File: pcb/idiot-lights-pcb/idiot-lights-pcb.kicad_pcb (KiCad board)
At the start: 2 copper layers, 100.3 x 64.1 mm, 103 parts, among them Q1 BSS138, Q10 BSS138, Q11 BSS138, Q12 BSS138, Q13 BSS138, Q14 BSS138, Q15 BSS138, Q16 BSS138, Q2 BSS138, Q3 BSS138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

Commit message: Fix resistor values
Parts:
- R10, R12, R14, R16, R18, R2, R20, R22, R24, R26, R28, R30, R32, R4, R6, R8: value 150 -> 330
- R33, R34, R35, R36, R37, R38, R39, R40, R41, R42, R43, R44, R45, R46, R47, R48: value 3k3 -> 1500
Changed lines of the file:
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@@
         (effects (font (size 1 1) (thickness 0.15)))
     )
-    (fp_text value "150" (at 0 1.43 180) (layer "F.Fab")
+    (fp_text value "330" (at 0 1.43 180) (layer "F.Fab")
         (effects (font (size 1 1) (thickness 0.15)))
     )
@@
         (effects (font (size 1 1) (thickness 0.15)))
     )
-    (fp_text value "150" (at 0 1.43 180) (layer "F.Fab")
+    (fp_text value "330" (at 0 1.43 180) (layer "F.Fab")
         (effects (font (size 1 1) (thickness 0.15)))
     )
@@
         (effects (font (size 1 1) (thickness 0.15)))
     )
-    (fp_text value "3k3" (at 0 1.43) (layer "F.Fab")
+    (fp_text value "1500" (at 0 1.43) (layer "F.Fab")
         (effects (font (size 1 1) (thickness 0.15)))
     )
@@
         (effects (font (size 1 1) (thickness 0.15)))
     )
-    (fp_text value "3k3" (at 0 1.43) (layer "F.Fab")
+    (fp_text value "1500" (at 0 1.43) (layer "F.Fab")
         (effects (font (size 1 1) (thickness 0.15)))
     )
@@
         (effects (font (size 1 1) (thickness 0.15)))
     )
-    (fp_text value "150" (at 0 1.43) (layer "F.Fab")
+    (fp_text value "330" (at 0 1.43) (layer "F.Fab")
         (effects (font (size 1 1) (thickness 0.15)))
     )
@@
         (effects (font (size 1 1) (thickness 0.15)))
     )
-    (fp_text value "3k3" (at 0 1.43) (layer "F.Fab")
+    (fp_text value "1500" (at 0 1.43) (layer "F.Fab")
         (effects (font (size 1 1) (thickness 0.15)))
     )
@@
         (effects (font (size 1 1) (thickness 0.15)))
     )
-    (fp_text value "3k3" (at 0 1.43) (layer "F.Fab")
+    (fp_text value "1500" (at 0 1.43) (layer "F.Fab")
         (effects (font (size 1 1) (thickness 0.15)))
     )
@@
         (effects (font (size 1 1) (thickness 0.15)))
     )
-    (fp_text value "3k3" (at 0 1.43) (layer "F.Fab")
+    (fp_text value "1500" (at 0 1.43) (layer "F.Fab")
         (effects (font (size 1 1) (thickness 0.15)))
     )
@@
         (effects (font (size 1 1) (thickness 0.15)))
     )
-    (fp_text value "3k3" (at 0 1.43) (layer "F.Fab")
+    (fp_text value "1500" (at 0 1.43) (layer "F.Fab")
         (effects (font (size 1 1) (thickness 0.15)))
     )
@@
         (effects (font (size 1 1) (thickness 0.15)))
     )
-    (fp_text value "3k3" (at 0 1.43) (layer "F.Fab")
+    (fp_text value "1500" (at 0 1.43) (layer "F.Fab")
         (effects (font (size 1 1) (thickness 0.15)))
     )
@@
         (effects (font (size 1 1) (thickness 0.15)))
     )
-    (fp_text value "150" (at 0 1.43 180) (layer "F.Fab")
+    (fp_text value "330" (at 0 1.43 180) (layer "F.Fab")
         (effects (font (size 1 1) (thickness 0.15)))
     )
@@
         (effects (font (size 1 1) (thickness 0.15)))
     )
-    (fp_text value "150" (at 0 1.43) (layer "F.Fab")
+    (fp_text value "330" (at 0 1.43) (layer "F.Fab")
         (effects (font (size 1 1) (thickness 0.15)))
     )
@@
         (effects (font (size 1 1) (thickness 0.15)))
     )
-    (fp_text value "150" (at 0 1.43) (layer "F.Fab")
+    (fp_text value "330" (at 0 1.43) (layer "F.Fab")
         (effects (font (size 1 1) (thickness 0.15)))
     )
@@
         (effects (font (size 1 1) (thickness 0.15)))
     )
-    (fp_text value "150" (at 0 1.43 180) (layer "F.Fab")
+    (fp_text value "330" (at 0 1.43 180) (layer "F.Fab")
         (effects (font (size 1 1) (thickness 0.15)))
     )
@@
         (effects (font (size 1 1) (thickness 0.15)))
     )
-    (fp_text value "150" (at 0 1.43) (layer "F.Fab")
+    (fp_text value "330" (at 0 1.43) (layer "F.Fab")
         (effects (font (size 1 1) (thickness 0.15)))
     )
@@
         (effects (font (size 1 1) (thickness 0.15)))
     )
-    (fp_text value "150" (at 0 1.43) (layer "F.Fab")
+    (fp_text value "330" (at 0 1.43) (layer "F.Fab")
         (effects (font (size 1 1) (thickness 0.15)))
     )
@@
         (effects (font (size 1 1) (thickness 0.15)))
     )
-    (fp_text value "150" (at 0 1.43) (layer "F.Fab")
+    (fp_text value "330" (at 0 1.43) (layer "F.Fab")
         (effects (font (size 1 1) (thickness 0.15)))
     )
@@
         (effects (font (size 1 1) (thickness 0.15)))
     )
-    (fp_text value "3k3" (at 0 1.43) (layer "F.Fab")
+    (fp_text value "1500" (at 0 1.43) (layer "F.Fab")
         (effects (font (size 1 1) (thickness 0.15)))
     )
@@
         (effects (font (size 1 1) (thickness 0.15)))
     )
-    (fp_text value "3k3" (at 0 1.43) (layer "F.Fab")
+    (fp_text value "1500" (at 0 1.43) (layer "F.Fab")
         (effects (font (size 1 1) (thickness 0.15)))
     )
@@
         (effects (font (size 1 1) (thickness 0.15)))
     )
-    (fp_text value "150" (at 0 1.43) (layer "F.Fab")
+    (fp_text value "330" (at 0 1.43) (layer "F.Fab")
         (effects (font (size 1 1) (thickness 0.15)))
     )
@@
         (effects (font (size 1 1) (thickness 0.15)))
     )
-    (fp_text value "150" (at 0 1.43) (layer "F.Fab")
+    (fp_text value "330" (at 0 1.43) (layer "F.Fab")
         (effects (font (size 1 1) (thickness 0.15)))
     )
@@
         (effects (font (size 1 1) (thickness 0.15)))
     )
-    (fp_text value "150" (at 0 1.43) (layer "F.Fab")
+    (fp_text value "330" (at 0 1.43) (layer "F.Fab")
         (effects (font (size 1 1) (thickness 0.15)))
     )
@@
         (effects (font (size 1 1) (thickness 0.15)))
     )
-    (fp_text value "150" (at 0 1.43) (layer "F.Fab")
+    (fp_text value "330" (at 0 1.43) (layer "F.Fab")
         (effects (font (size 1 1) (thickness 0.15)))
     )
@@
         (effects (font (size 1 1) (thickness 0.15)))
     )
-    (fp_text value "3k3" (at 0 1.43) (layer "F.Fab")
+    (fp_text value "1500" (at 0 1.43) (layer "F.Fab")
         (effects (font (size 1 1) (thickness 0.15)))
     )
@@
     (fp_arc (start 10 -25.61) (mid 10.357937 -25.493944) (end 10.579676 -25.189937)
       (stroke (width 0.12) (type solid)) (layer "F.SilkS"))
-    (fp_arc (start 10.579676 25.189937) (mid 10.357958 25.493991) (end 10 25.61)
+    (fp_arc (start 10.579676 25.189937) (mid 10.35796 25.493961) (end 10 25.61)
       (stroke (width 0.12) (type solid)) (layer "F.SilkS"))
     (fp_circle (center -5.7 -23.5) (end -4.76 -23.5)
@@
         (effects (font (size 1 1) (thickness 0.15)))
     )
-    (fp_text value "3k3" (at 0 1.43) (layer "F.Fab") hide
+    (fp_text value "1500" (at 0 1.43) (layer "F.Fab") hide
         (effects (font (size 1 1) (thickness 0.15)))
     )
@@
         (effects (font (size 1 1) (thickness 0.15)))
     )
-    (fp_text value "3k3" (at 0 1.43) (layer "F.Fab")
+    (fp_text value "1500" (at 0 1.43) (layer "F.Fab")
         (effects (font (size 1 1) (thickness 0.15)))
     )
@@
         (effects (font (size 1 1) (thickness 0.15)))
     )
-    (fp_text value "3k3" (at 0 1.43) (layer "F.Fab")
+    (fp_text value "1500" (at 0 1.43) (layer "F.Fab")
         (effects (font (size 1 1) (thickness 0.15)))
     )
@@
         (effects (font (size 1 1) (thickness 0.15)))
     )
-    (fp_text value "150" (at 0 1.43) (layer "F.Fab")
+    (fp_text value "330" (at 0 1.43) (layer "F.Fab")
         (effects (font (size 1 1) (thickness 0.15)))
     )
@@
         (effects (font (size 1 1) (thickness 0.15)))
     )
-    (fp_text value "150" (at 0 1.43) (layer "F.Fab")
+    (fp_text value "330" (at 0 1.43) (layer "F.Fab")
         (effects (font (size 1 1) (thickness 0.15)))
     )
@@
         (effects (font (size 1 1) (thickness 0.15)))
     )
-    (fp_text value "3k3" (at 0 1.43) (layer "F.Fab")
+    (fp_text value "1500" (at 0 1.43) (layer "F.Fab")
         (effects (font (size 1 1) (thickness 0.15)))
     )
@@
         (effects (font (size 1 1) (thickness 0.15)))
     )
-    (fp_text value "3k3" (at 0 1.43) (layer "F.Fab")
+    (fp_text value "1500" (at 0 1.43) (layer "F.Fab")
         (effects (font (size 1 1) (thickness 0.15)))
     )
@@
         (effects (font (size 1 1) (thickness 0.15)))
     )
-    (fp_text value "3k3" (at 0 1.43) (layer "F.Fab")
+    (fp_text value "1500" (at 0 1.43) (layer "F.Fab")
         (effects (font (size 1 1) (thickness 0.15)))
     )

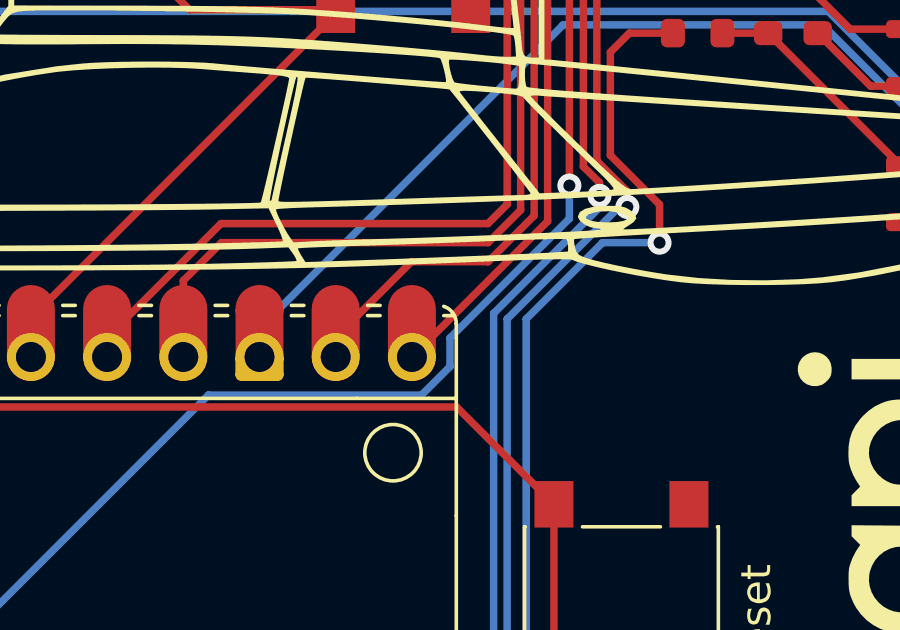
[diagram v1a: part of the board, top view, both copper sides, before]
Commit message: Increase LED resistor values - dim LEDs
Set RPI pico property to THT again
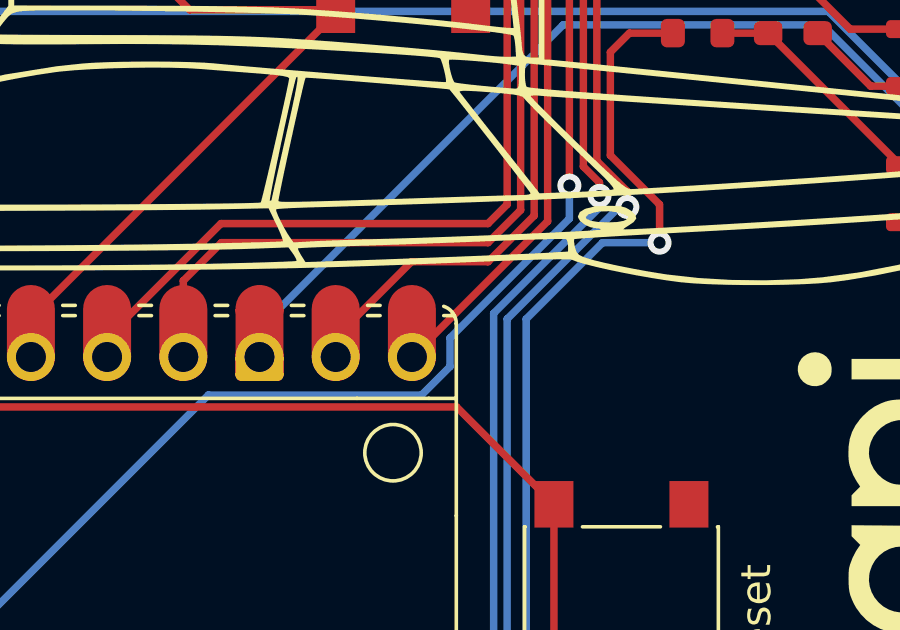
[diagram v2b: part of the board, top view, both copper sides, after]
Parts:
- R10, R12, R14, R16, R18, R2, R20, R22, R24, R26, R28, R30, R32, R4, R6, R8: value 330 -> 10k
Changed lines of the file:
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@@
         (effects (font (size 1 1) (thickness 0.15)))
     )
-    (fp_text value "330" (at 0 1.43 180) (layer "F.Fab")
+    (fp_text value "10k" (at 0 1.43 180) (layer "F.Fab")
         (effects (font (size 1 1) (thickness 0.15)))
     )
@@
         (effects (font (size 1 1) (thickness 0.15)))
     )
-    (fp_text value "330" (at 0 1.43 180) (layer "F.Fab")
+    (fp_text value "10k" (at 0 1.43 180) (layer "F.Fab")
         (effects (font (size 1 1) (thickness 0.15)))
     )
@@
         (effects (font (size 1 1) (thickness 0.15)))
     )
-    (fp_text value "330" (at 0 1.43) (layer "F.Fab")
+    (fp_text value "10k" (at 0 1.43) (layer "F.Fab")
         (effects (font (size 1 1) (thickness 0.15)))
     )
@@
         (effects (font (size 1 1) (thickness 0.15)))
     )
-    (fp_text value "330" (at 0 1.43 180) (layer "F.Fab")
+    (fp_text value "10k" (at 0 1.43 180) (layer "F.Fab")
         (effects (font (size 1 1) (thickness 0.15)))
     )
@@
         (effects (font (size 1 1) (thickness 0.15)))
     )
-    (fp_text value "330" (at 0 1.43) (layer "F.Fab")
+    (fp_text value "10k" (at 0 1.43) (layer "F.Fab")
         (effects (font (size 1 1) (thickness 0.15)))
     )
@@
         (effects (font (size 1 1) (thickness 0.15)))
     )
-    (fp_text value "330" (at 0 1.43) (layer "F.Fab")
+    (fp_text value "10k" (at 0 1.43) (layer "F.Fab")
         (effects (font (size 1 1) (thickness 0.15)))
     )
@@
         (effects (font (size 1 1) (thickness 0.15)))
     )
-    (fp_text value "330" (at 0 1.43 180) (layer "F.Fab")
+    (fp_text value "10k" (at 0 1.43 180) (layer "F.Fab")
         (effects (font (size 1 1) (thickness 0.15)))
     )
@@
         (effects (font (size 1 1) (thickness 0.15)))
     )
-    (fp_text value "330" (at 0 1.43) (layer "F.Fab")
+    (fp_text value "10k" (at 0 1.43) (layer "F.Fab")
         (effects (font (size 1 1) (thickness 0.15)))
     )
@@
         (effects (font (size 1 1) (thickness 0.15)))
     )
-    (fp_text value "330" (at 0 1.43) (layer "F.Fab")
+    (fp_text value "10k" (at 0 1.43) (layer "F.Fab")
         (effects (font (size 1 1) (thickness 0.15)))
     )
@@
         (effects (font (size 1 1) (thickness 0.15)))
     )
-    (fp_text value "330" (at 0 1.43) (layer "F.Fab")
+    (fp_text value "10k" (at 0 1.43) (layer "F.Fab")
         (effects (font (size 1 1) (thickness 0.15)))
     )
@@
         (effects (font (size 1 1) (thickness 0.15)))
     )
-    (fp_text value "330" (at 0 1.43) (layer "F.Fab")
+    (fp_text value "10k" (at 0 1.43) (layer "F.Fab")
         (effects (font (size 1 1) (thickness 0.15)))
     )
@@
         (effects (font (size 1 1) (thickness 0.15)))
     )
-    (fp_text value "330" (at 0 1.43) (layer "F.Fab")
+    (fp_text value "10k" (at 0 1.43) (layer "F.Fab")
         (effects (font (size 1 1) (thickness 0.15)))
     )
@@
         (effects (font (size 1 1) (thickness 0.15)))
     )
-    (fp_text value "330" (at 0 1.43) (layer "F.Fab")
+    (fp_text value "10k" (at 0 1.43) (layer "F.Fab")
         (effects (font (size 1 1) (thickness 0.15)))
     )
@@
         (effects (font (size 1 1) (thickness 0.15)))
     )
-    (fp_text value "330" (at 0 1.43) (layer "F.Fab")
+    (fp_text value "10k" (at 0 1.43) (layer "F.Fab")
         (effects (font (size 1 1) (thickness 0.15)))
     )
@@
     (fp_arc (start 10 -25.61) (mid 10.357937 -25.493944) (end 10.579676 -25.189937)
       (stroke (width 0.12) (type solid)) (layer "F.SilkS"))
-    (fp_arc (start 10.579676 25.189937) (mid 10.35796 25.493961) (end 10 25.61)
+    (fp_arc (start 10.579676 25.189937) (mid 10.357946 25.493957) (end 10 25.61)
       (stroke (width 0.12) (type solid)) (layer "F.SilkS"))
     (fp_circle (center -5.7 -23.5) (end -4.76 -23.5)
@@
         (effects (font (size 1 1) (thickness 0.15)))
     )
-    (fp_text value "330" (at 0 1.43) (layer "F.Fab")
+    (fp_text value "10k" (at 0 1.43) (layer "F.Fab")
         (effects (font (size 1 1) (thickness 0.15)))
     )
@@
         (effects (font (size 1 1) (thickness 0.15)))
     )
-    (fp_text value "330" (at 0 1.43) (layer "F.Fab")
+    (fp_text value "10k" (at 0 1.43) (layer "F.Fab")
         (effects (font (size 1 1) (thickness 0.15)))
     )

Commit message: Bump pcb version
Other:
- board text added: "turn-cygnicator v.1.3"
- board text removed: "turn-cygnicator v.1.2"
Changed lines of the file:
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@@
     (fp_arc (start 10 -25.61) (mid 10.357937 -25.493944) (end 10.579676 -25.189937)
       (stroke (width 0.12) (type solid)) (layer "F.SilkS"))
-    (fp_arc (start 10.579676 25.189937) (mid 10.357946 25.493957) (end 10 25.61)
+    (fp_arc (start 10.579676 25.189937) (mid 10.357958 25.493991) (end 10 25.61)
       (stroke (width 0.12) (type solid)) (layer "F.SilkS"))
     (fp_circle (center -5.7 -23.5) (end -4.76 -23.5)
@@
     )
   )
-  (gr_text "turn-cygnicator v.1.2" (at 226.06 99.06 90) (layer "F.SilkS")
+  (gr_text "turn-cygnicator v.1.3" (at 226.06 99.06 90) (layer "F.SilkS")
     (effects (font (size 1 1) (thickness 0.25) bold) (justify left bottom))
   )

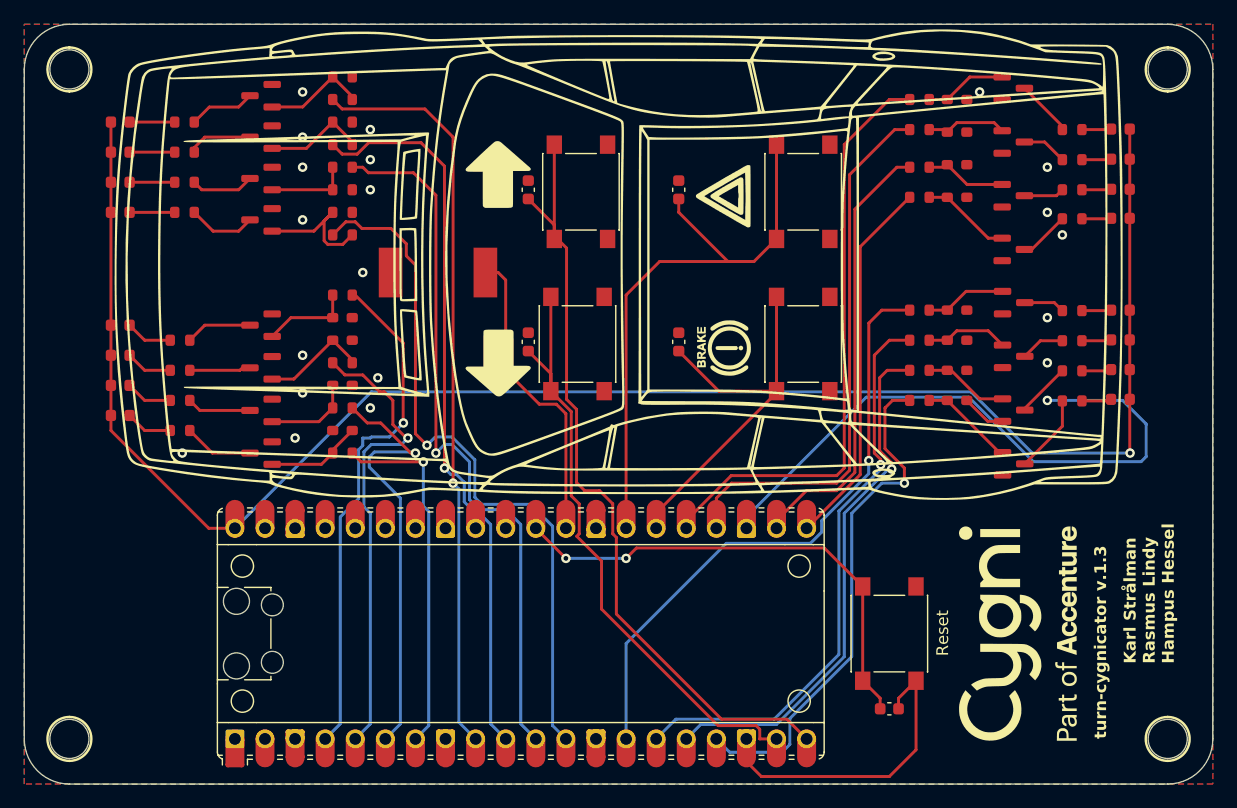
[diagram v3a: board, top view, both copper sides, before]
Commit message: Add smaller QR code and remove corner for usb cable
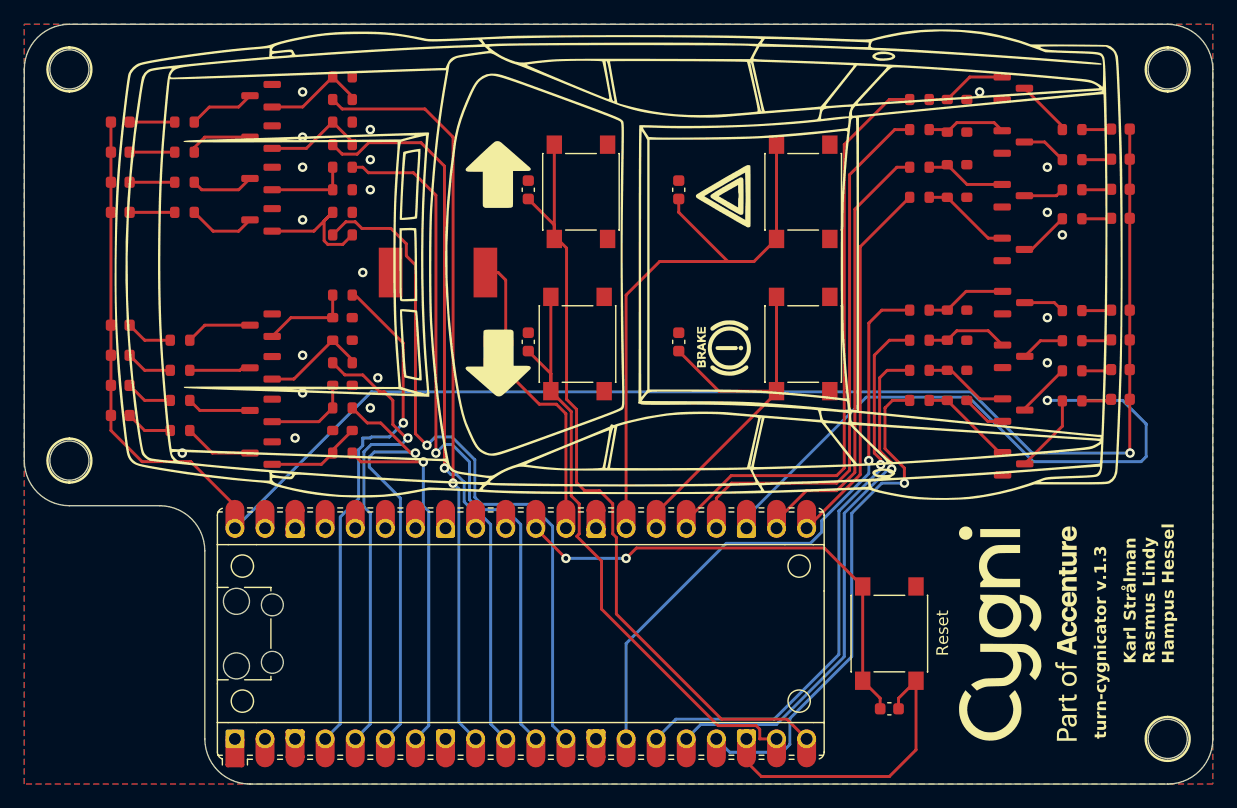
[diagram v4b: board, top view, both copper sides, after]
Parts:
- removed the G*** at (185.4, 70.5)
- added G***: LOGO, cts-qr-code:qr_45x45, B.Cu at (183.5, 70.5)
- moved >NAME 23.5 mm to (138.4, 75.6)
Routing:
- net +5V: track 149.8 -> 150.9 mm
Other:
- outline, holes or cut-outs redrawn
